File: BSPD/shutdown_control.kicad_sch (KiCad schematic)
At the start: 9 parts, among them K2 G6BK-1114P-US, U16 TLP3122AE, U26 DK1A1B-12V, U27 TLP3122AE

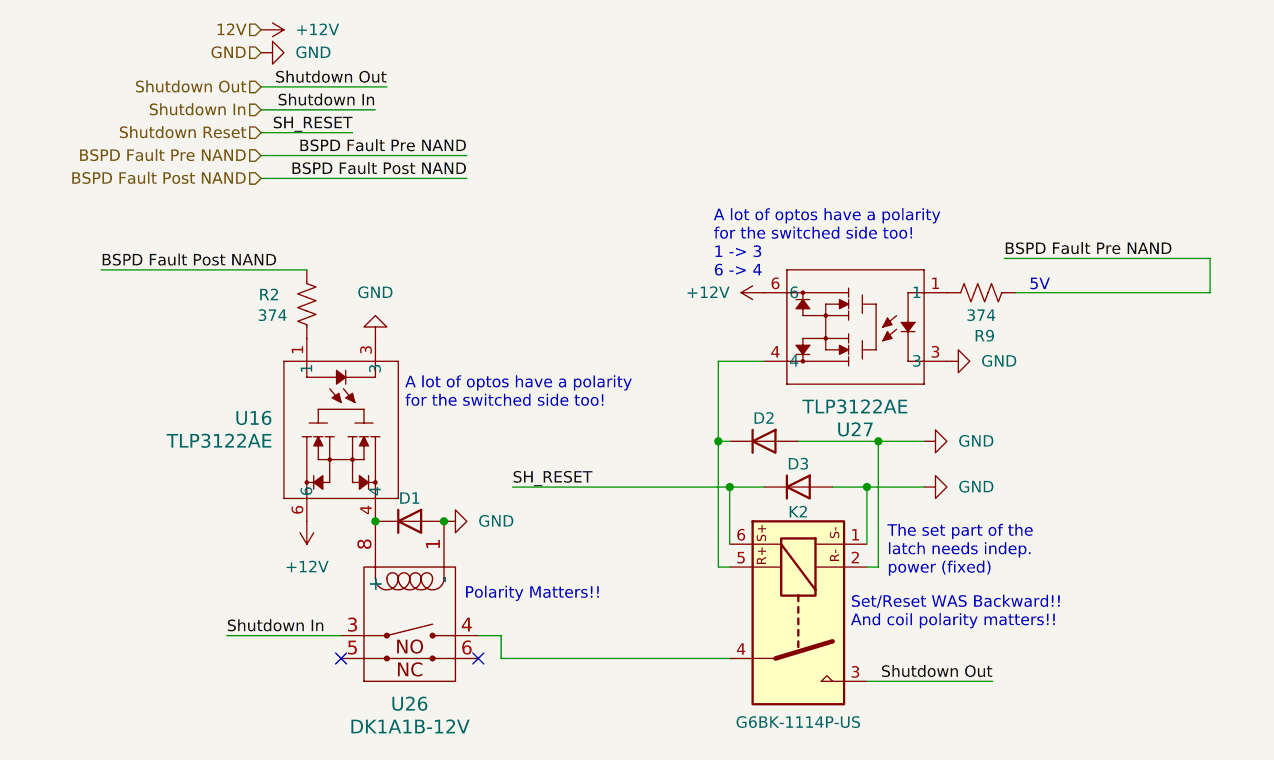
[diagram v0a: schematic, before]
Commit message: Overhaul of BPSD to V3.0
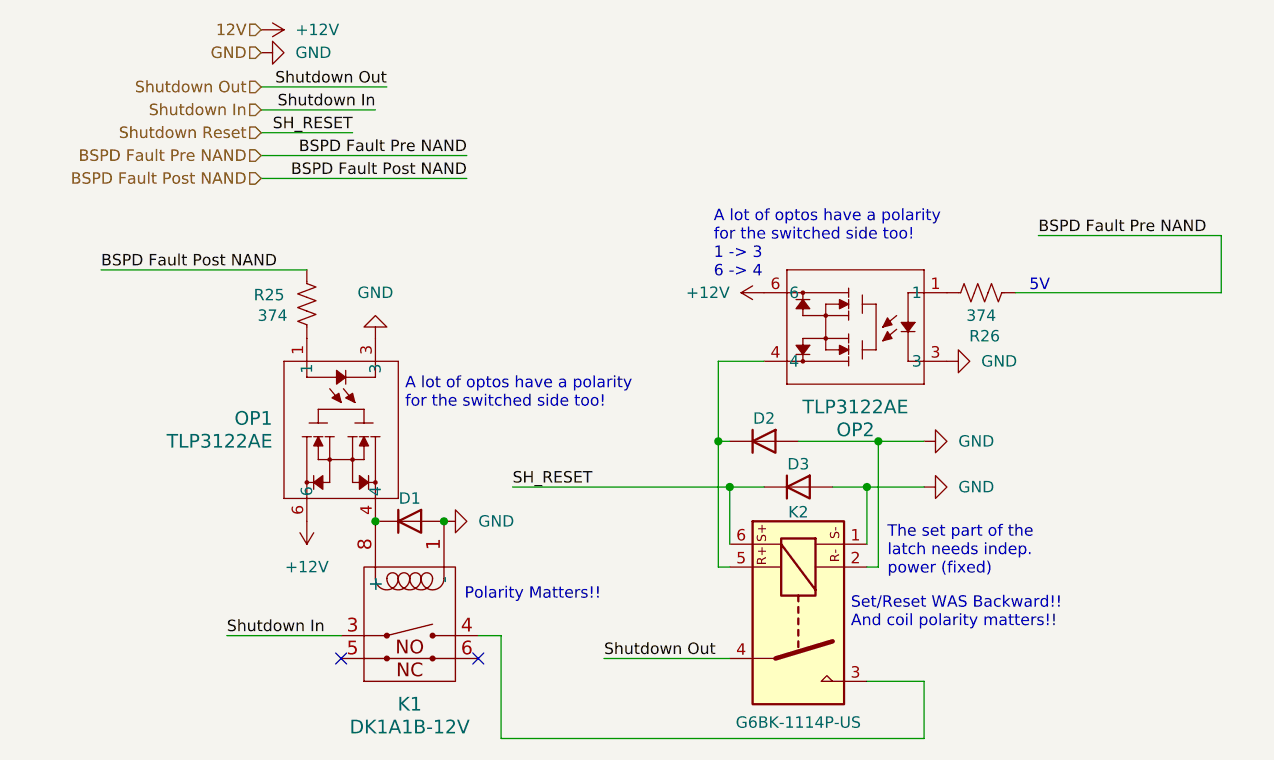
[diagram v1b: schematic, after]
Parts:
- renumbered U26 to K1, U16 to OP1, U27 to OP2, R2 to R25, R9 to R26
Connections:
- net Shutdown Out: now also K2.4; no longer K2.3
- net at K1.4: now also K2.3; no longer K2.4
